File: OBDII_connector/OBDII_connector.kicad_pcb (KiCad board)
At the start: 2 copper layers, 34 x 16 mm, 9 parts, among them J1 Conn_02x08_Counter_Clockwise, J2 Conn_01x02

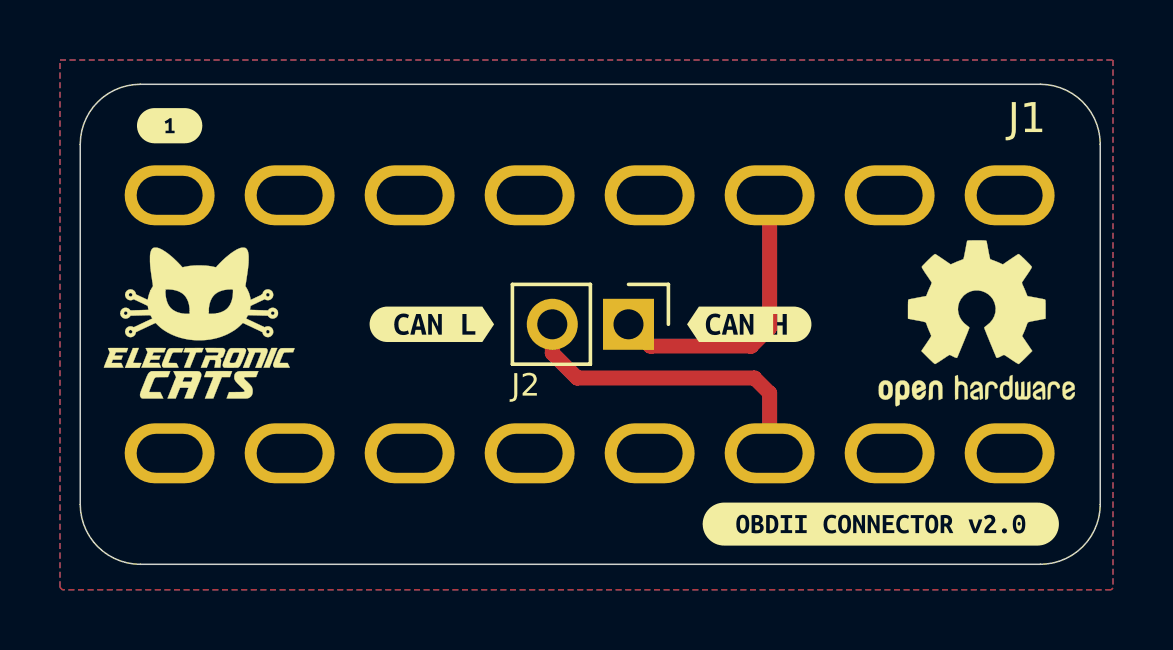
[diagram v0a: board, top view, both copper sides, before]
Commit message: feat: add GND between OBDII connector & OBDII_RJ45
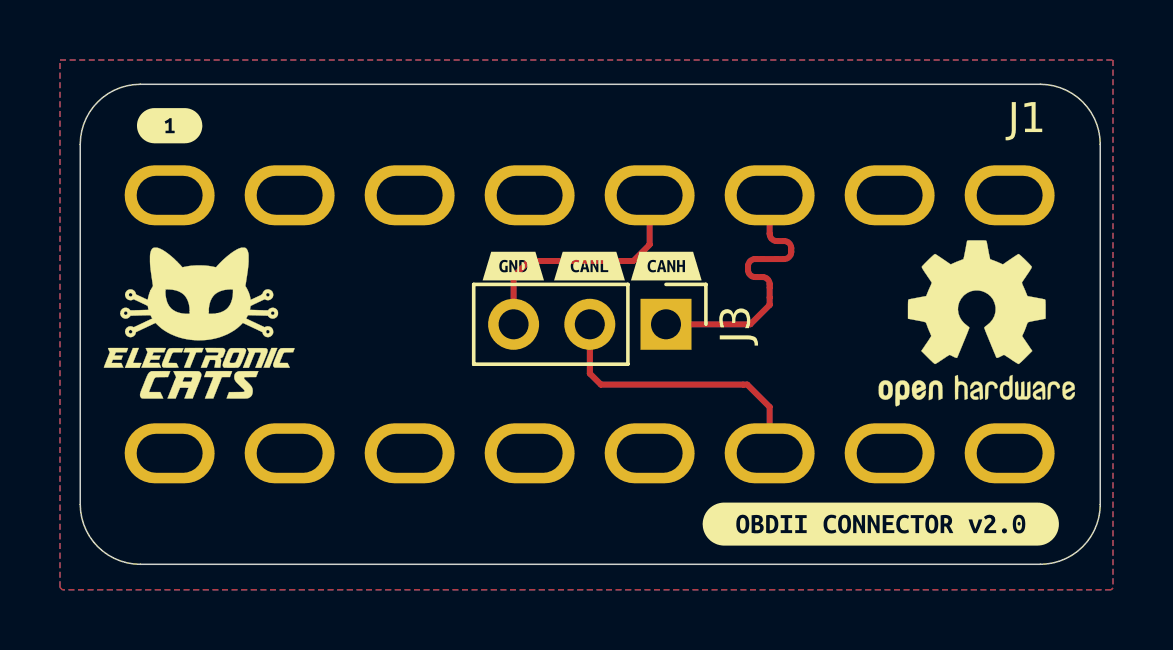
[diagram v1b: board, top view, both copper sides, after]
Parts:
- removed J2: Conn_01x02, Connector_PinHeader_2.54mm:PinHeader_1x02_P2.54mm_Vertical
- removed kibuzzard-6646749E: G***, kibuzzard-6646749E
- removed kibuzzard-66467618: G***, kibuzzard-66467618
- added J3: Conn_01x03, Connector_PinHeader_2.54mm:PinHeader_1x03_P2.54mm_Vertical, F.Cu at (152.2, 51.2)
- added kibuzzard-67DDAD0A: G***, kibuzzard-67DDAD0A, F.Cu at (149.7, 49.3)
- added kibuzzard-67DDAD2E: G***, kibuzzard-67DDAD2E, F.Cu at (152.3, 49.3)
- added kibuzzard-67DDAD71: G***, kibuzzard-67DDAD71, F.Cu at (147.2, 49.3)
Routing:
- net GND: track 0.00 -> 8.22 mm
- net /CAN_L: track 10.8 -> 9.64 mm

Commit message: feat(Hw):Update_Labels
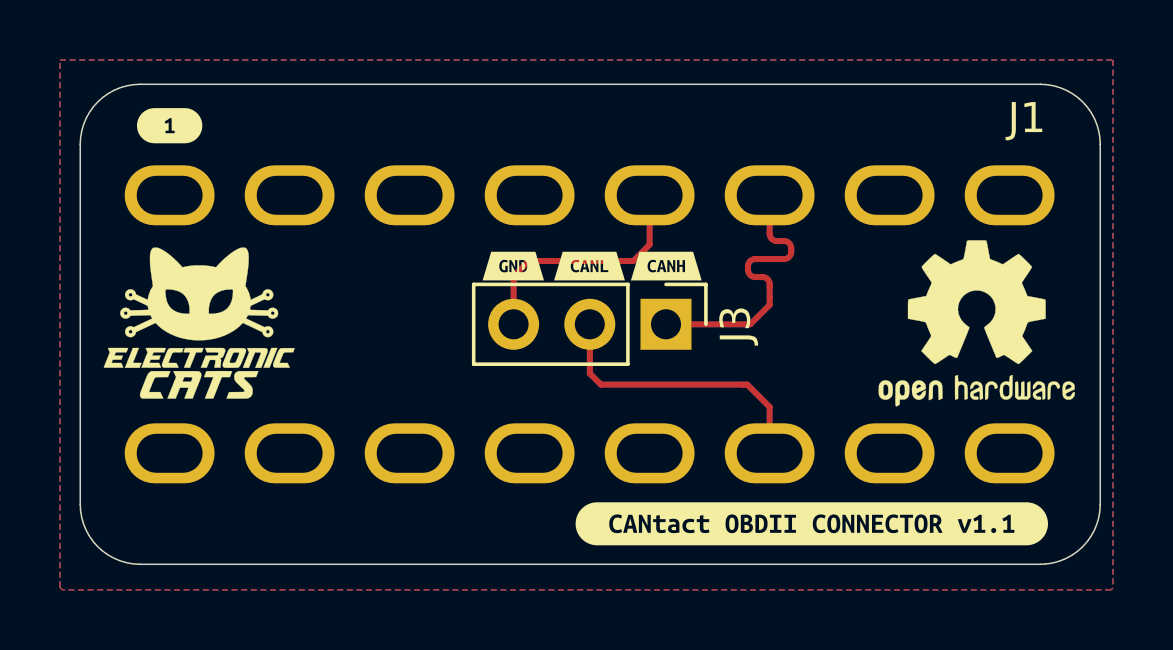
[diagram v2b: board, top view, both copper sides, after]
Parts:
- removed kibuzzard-66AA65F0: G***, kibuzzard-66AA65F0
- added kibuzzard-67FE8BBD: G***, kibuzzard-67FE8BBD, F.Cu at (157.1, 57.9)
